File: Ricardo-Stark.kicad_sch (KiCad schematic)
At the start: 54 parts, among them J1 RBUS, U1 ESP32-S3, Y1 R940000171

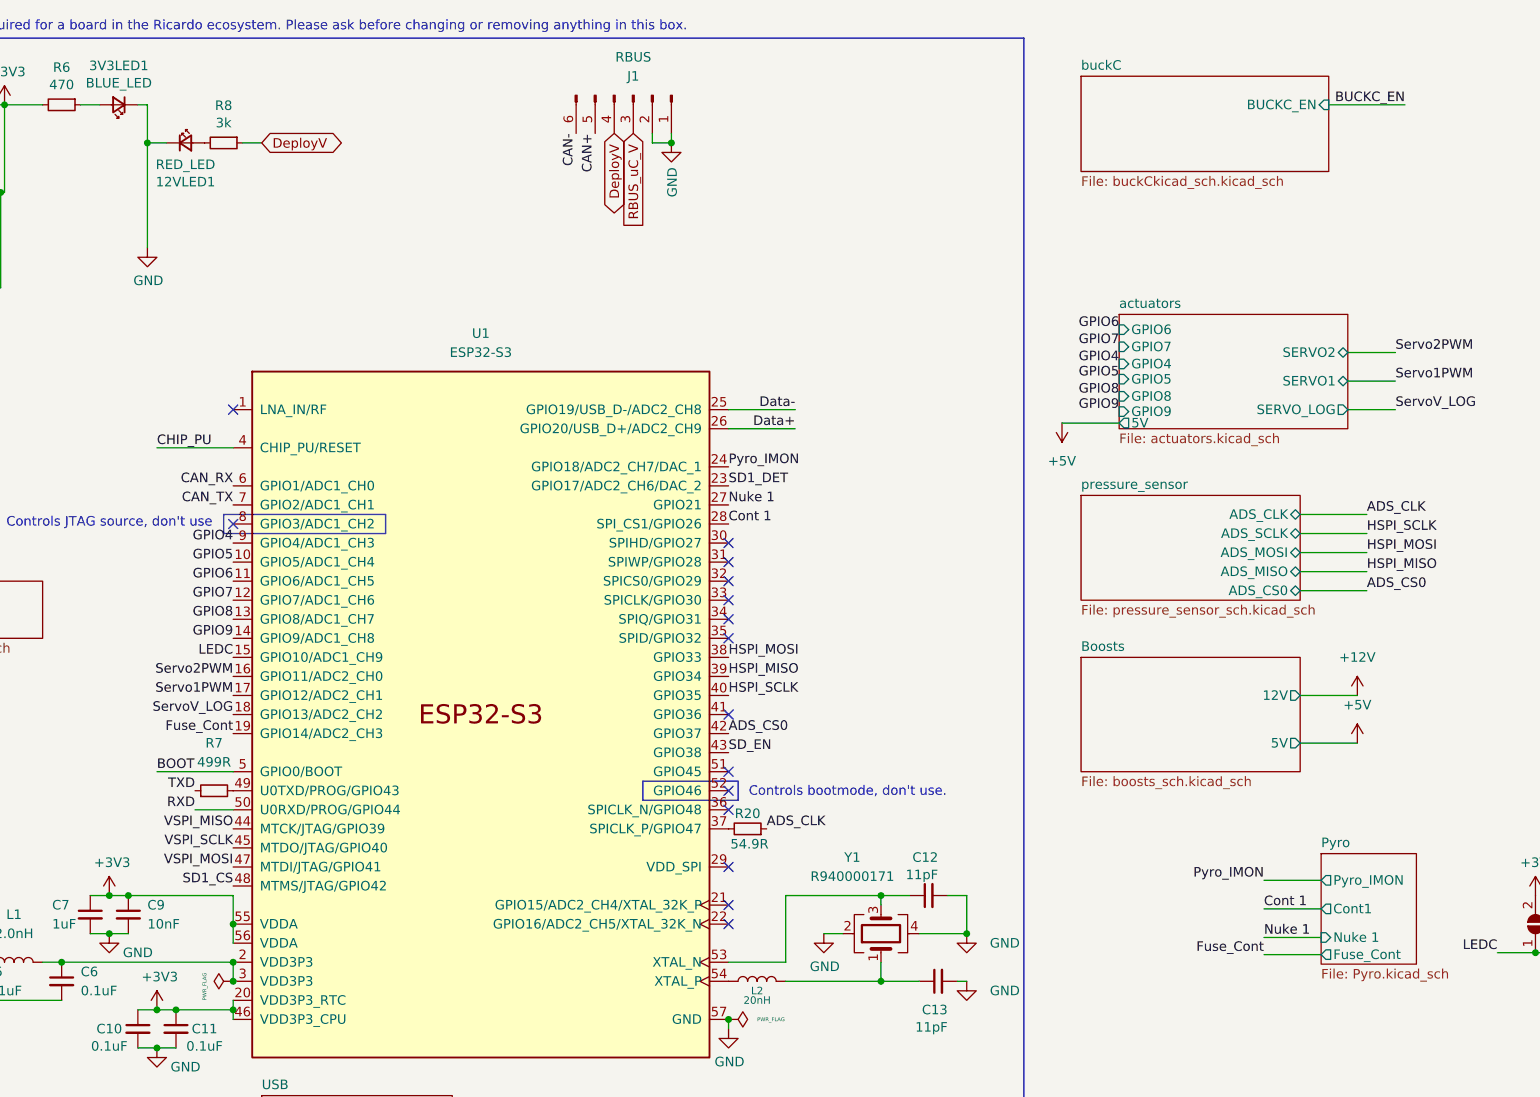
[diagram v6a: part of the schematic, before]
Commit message: reshuffled layout
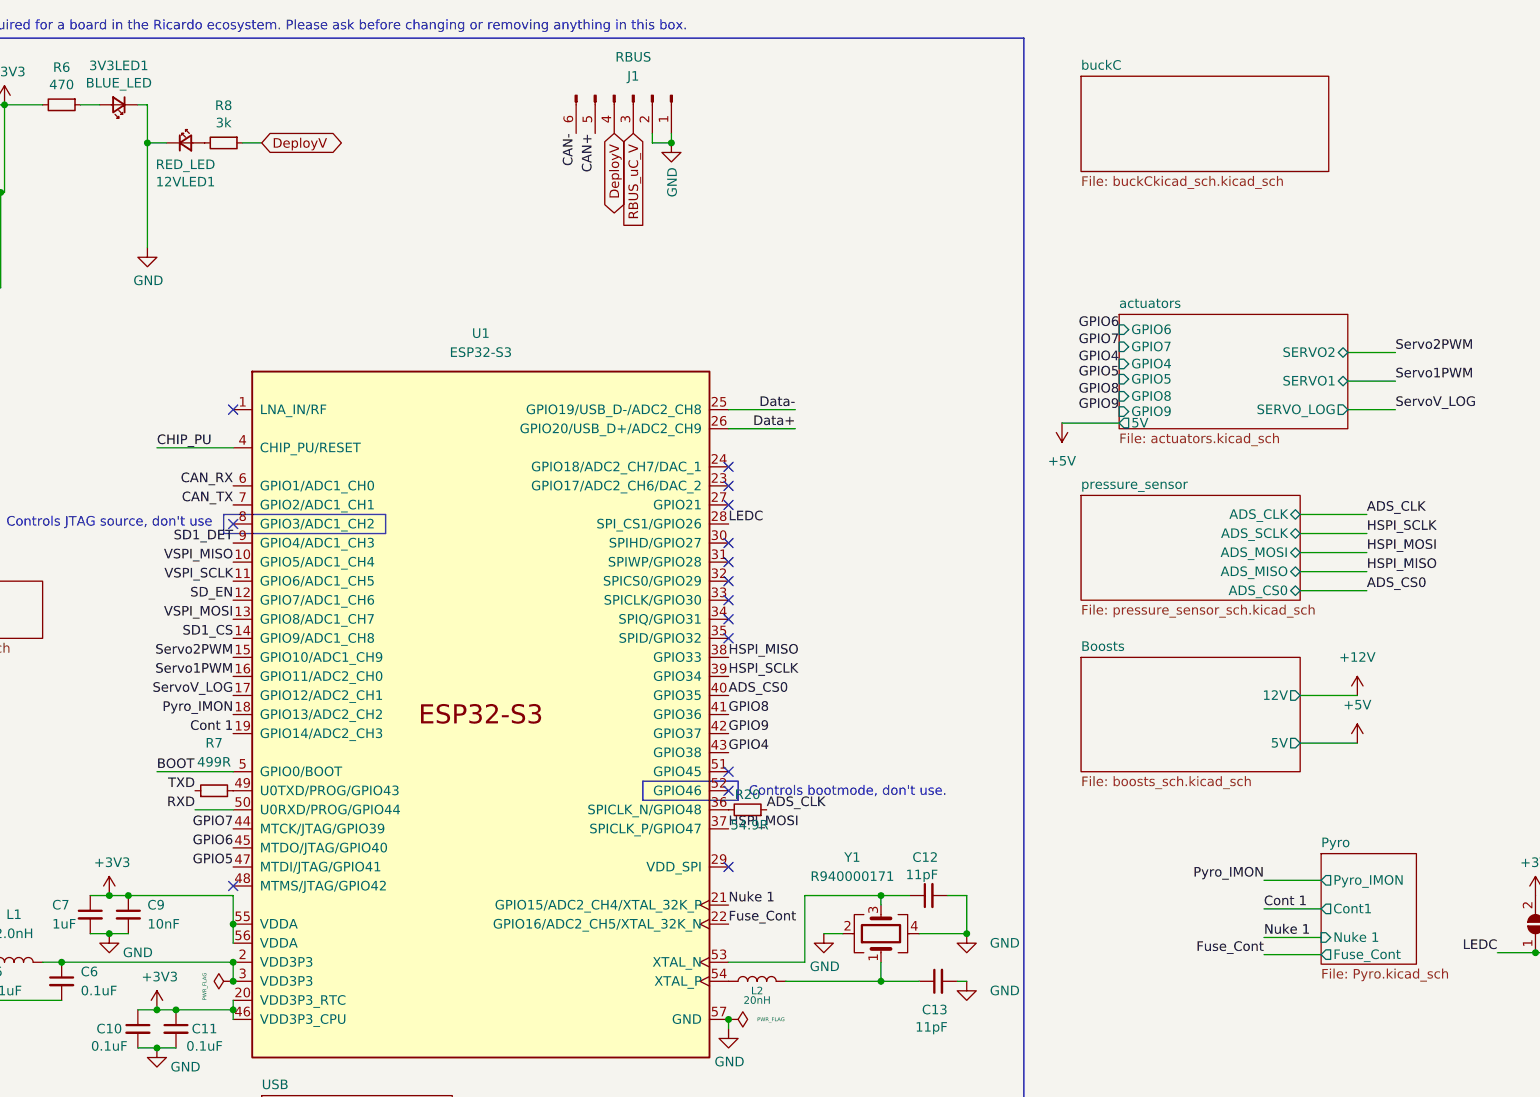
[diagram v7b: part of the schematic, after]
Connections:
- net ADS_CS0: now also U1.40 (GPIO35); no longer U1.42 (GPIO37)
- net Cont 1: now also U1.19 (GPIO14/ADC2_CH3); no longer U1.28 (SPI_CS1/GPIO26)
- net Fuse_Cont: now also U1.22 (GPIO16/ADC2_CH5/XTAL_32K_N); no longer U1.19 (GPIO14/ADC2_CH3)
- net GPIO4: now also U1.43 (GPIO38); no longer U1.9 (GPIO4/ADC1_CH3)
- net GPIO5: now also U1.47 (MTDI/JTAG/GPIO41); no longer U1.10 (GPIO5/ADC1_CH4)
- net GPIO6: now also U1.45 (MTDO/JTAG/GPIO40); no longer U1.11 (GPIO6/ADC1_CH5)
- net GPIO7: now also U1.44 (MTCK/JTAG/GPIO39); no longer U1.12 (GPIO7/ADC1_CH6)
- net GPIO8: now also U1.41 (GPIO36); no longer U1.13 (GPIO8/ADC1_CH7)
- net GPIO9: now also U1.42 (GPIO37); no longer U1.14 (GPIO9/ADC1_CH8)
- net HSPI_MISO: now also U1.38 (GPIO33); no longer U1.39 (GPIO34)
- net HSPI_MOSI: now also U1.37 (SPICLK_P/GPIO47); no longer U1.38 (GPIO33)
- net HSPI_SCLK: now also U1.39 (GPIO34); no longer U1.40 (GPIO35)
- net LEDC: now also U1.28 (SPI_CS1/GPIO26); no longer U1.15 (GPIO10/ADC1_CH9)
- net Nuke 1: now also U1.21 (GPIO15/ADC2_CH4/XTAL_32K_P); no longer U1.27 (GPIO21)
- net Pyro_IMON: now also U1.18 (GPIO13/ADC2_CH2); no longer U1.24 (GPIO18/ADC2_CH7/DAC_1)
- net SD1_CS: now also U1.14 (GPIO9/ADC1_CH8); no longer U1.48 (MTMS/JTAG/GPIO42)
- net SD1_DET: now also U1.9 (GPIO4/ADC1_CH3); no longer U1.23 (GPIO17/ADC2_CH6/DAC_2)
- net SD_EN: now also U1.12 (GPIO7/ADC1_CH6); no longer U1.43 (GPIO38)
- net Servo1PWM: now also U1.16 (GPIO11/ADC2_CH0); no longer U1.17 (GPIO12/ADC2_CH1)
- net Servo2PWM: now also U1.15 (GPIO10/ADC1_CH9); no longer U1.16 (GPIO11/ADC2_CH0)
- net ServoV_LOG: now also U1.17 (GPIO12/ADC2_CH1); no longer U1.18 (GPIO13/ADC2_CH2)
- net VSPI_MISO: now also U1.10 (GPIO5/ADC1_CH4); no longer U1.44 (MTCK/JTAG/GPIO39)
- net VSPI_MOSI: now also U1.13 (GPIO8/ADC1_CH7); no longer U1.47 (MTDI/JTAG/GPIO41)
- net VSPI_SCLK: now also U1.11 (GPIO6/ADC1_CH5); no longer U1.45 (MTDO/JTAG/GPIO40)
- net at R20.2: now also U1.36 (SPICLK_N/GPIO48); no longer U1.37 (SPICLK_P/GPIO47)
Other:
- sheet buckC ports: added none; removed BUCKC_EN
- moved on the sheet: R20
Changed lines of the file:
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@@
 	)
 	(no_connect
+		(at 135.89 69.85)
+	)
+	(no_connect
 		(at 135.89 82.55)
 	)
 	(no_connect
-		(at 135.89 130.81)
+		(at 135.89 72.39)
 	)
 	(no_connect
@@
 	)
 	(no_connect
-		(at 135.89 128.27)
-	)
-	(no_connect
 		(at 135.89 90.17)
 	)
@@
 	)
 	(no_connect
+		(at 135.89 74.93)
+	)
+	(no_connect
 		(at 135.89 87.63)
 	)
@@
 	)
 	(no_connect
-		(at 135.89 115.57)
-	)
-	(no_connect
 		(at 135.89 123.19)
 	)
@@
 	)
 	(no_connect
-		(at 135.89 102.87)
+		(at 69.85 125.73)
 	)
 	(wire
@@
 	(wire
 		(pts
-			(xy 143.51 135.89) (xy 143.51 127)
+			(xy 146.05 135.89) (xy 146.05 127)
 		)
 		(stroke
@@
 	(wire
 		(pts
-			(xy 215.9 21.59) (xy 226.06 21.59)
-		)
-		(stroke
-			(width 0)
-			(type default)
-		)
-	)
-	(wire
-		(pts
 			(xy 107.95 187.96) (xy 115.57 187.96)
 		)
@@
 	(wire
 		(pts
-			(xy 135.89 135.89) (xy 143.51 135.89)
+			(xy 135.89 135.89) (xy 146.05 135.89)
 		)
 		(stroke
@@
 	(wire
 		(pts
-			(xy 143.51 127) (xy 156.21 127)
+			(xy 146.05 127) (xy 156.21 127)
 		)
 		(stroke
@@
 	)
 	(label "SD1_DET"
-		(at 135.89 72.39 0)
-		(fields_autoplaced yes)
-		(effects
-			(font
-				(size 1.27 1.27)
-			)
-			(justify left bottom)
-		)
-	)
-	(label "BUCKC_EN"
-		(at 226.06 21.59 180)
+		(at 69.85 80.01 180)
 		(fields_autoplaced yes)
 		(effects
@@
 	)
 	(label "SD_EN"
-		(at 135.89 107.95 0)
+		(at 69.85 87.63 180)
 		(fields_autoplaced yes)
 		(effects
@@
 				(size 1.27 1.27)
 			)
-			(justify left bottom)
+			(justify right bottom)
 		)
 	)
@@
 	)
 	(label "Servo2PWM"
-		(at 69.85 97.79 180)
+		(at 69.85 95.25 180)
 		(fields_autoplaced yes)
 		(effects
@@
 	)
 	(label "Pyro_IMON"
-		(at 135.89 69.85 0)
+		(at 69.85 102.87 180)
 		(fields_autoplaced yes)
 		(effects
@@
 				(size 1.27 1.27)
 			)
-			(justify left bottom)
+			(justify right bottom)
 		)
 	)
@@
 	)
 	(label "Servo1PWM"
-		(at 69.85 100.33 180)
+		(at 69.85 97.79 180)
 		(fields_autoplaced yes)
 		(effects
@@
 	)
 	(label "GPIO7"
-		(at 69.85 87.63 180)
+		(at 69.85 118.11 180)
 		(fields_autoplaced yes)
 		(effects
@@
 	)
 	(label "VSPI_SCLK"
-		(at 69.85 120.65 180)
+		(at 69.85 85.09 180)
 		(fields_autoplaced yes)
 		(effects
@@
 	)
 	(label "SD1_CS"
-		(at 69.85 125.73 180)
+		(at 69.85 92.71 180)
 		(fields_autoplaced yes)
 		(effects
@@
 	)
 	(label "GPIO9"
-		(at 69.85 92.71 180)
+		(at 135.89 105.41 0)
 		(fields_autoplaced yes)
 		(effects
@@
 				(size 1.27 1.27)
 			)
-			(justify right bottom)
+			(justify left bottom)
 		)
 	)
 	(label "HSPI_SCLK"
-		(at 135.89 100.33 0)
+		(at 135.89 97.79 0)
 		(fields_autoplaced yes)
 		(effects
@@
 	)
 	(label "Fuse_Cont"
-		(at 69.85 105.41 180)
+		(at 135.89 130.81 0)
 		(fields_autoplaced yes)
 		(effects
@@
 				(size 1.27 1.27)
 			)
-			(justify right bottom)
+			(justify left bottom)
 		)
 	)
 	(label "VSPI_MISO"
-		(at 69.85 118.11 180)
+		(at 69.85 82.55 180)
 		(fields_autoplaced yes)
 		(effects
@@
 	)
 	(label "ADS_CLK"
-		(at 140.97 118.11 0)
+		(at 140.97 115.57 0)
 		(fields_autoplaced yes)
 		(effects
@@
 	)
 	(label "LEDC"
-		(at 69.85 95.25 180)
+		(at 135.89 77.47 0)
 		(fields_autoplaced yes)
 		(effects
@@
 				(size 1.27 1.27)
 			)
-			(justify right bottom)
+			(justify left bottom)
 		)
 	)
@@
 	)
 	(label "GPIO8"
-		(at 69.85 90.17 180)
+		(at 135.89 102.87 0)
 		(fields_autoplaced yes)
 		(effects
@@
 				(size 1.27 1.27)
 			)
-			(justify right bottom)
+			(justify left bottom)
 		)
 	)
@@
 	)
 	(label "Cont 1"
-		(at 135.89 77.47 0)
+		(at 69.85 105.41 180)
 		(fields_autoplaced yes)
 		(effects
@@
 				(size 1.27 1.27)
 			)
-			(justify left bottom)
+			(justify right bottom)
 		)
 	)
@@
 	)
 	(label "ServoV_LOG"
-		(at 69.85 102.87 180)
+		(at 69.85 100.33 180)
 		(fields_autoplaced yes)
 		(effects
@@
 	)
 	(label "GPIO5"
-		(at 69.85 82.55 180)
+		(at 69.85 123.19 180)
 		(fields_autoplaced yes)
 		(effects
@@
 	)
 	(label "GPIO6"
-		(at 69.85 85.09 180)
+		(at 69.85 120.65 180)
 		(fields_autoplaced yes)
 		(effects
@@
 	)
 	(label "ADS_CS0"
-		(at 135.89 105.41 0)
+		(at 135.89 100.33 0)
 		(fields_autoplaced yes)
 		(effects
@@
 	)
 	(label "Nuke 1"
-		(at 135.89 74.93 0)
+		(at 135.89 128.27 0)
 		(fields_autoplaced yes)
 		(effects
@@
 	)
 	(label "VSPI_MOSI"
-		(at 69.85 123.19 180)
+		(at 69.85 90.17 180)
 		(fields_autoplaced yes)
 		(effects
@@
 	)
 	(label "GPIO4"
-		(at 69.85 80.01 180)
+		(at 135.89 107.95 0)
 		(fields_autoplaced yes)
 		(effects
@@
 				(size 1.27 1.27)
 			)
-			(justify right bottom)
+			(justify left bottom)
 		)
 	)
@@
 	)
 	(label "HSPI_MISO"
-		(at 135.89 97.79 0)
+		(at 135.89 95.25 0)
 		(fields_autoplaced yes)
 		(effects
@@
 	)
 	(label "HSPI_MOSI"
-		(at 135.89 95.25 0)
+		(at 135.89 118.11 0)
 		(fields_autoplaced yes)
 		(effects
@@
 	(symbol
 		(lib_id "Device:R_Small")
-		(at 138.43 118.11 270)
+		(at 138.43 115.57 270)
 		(mirror x)
 		(unit 1)
@@
 		(dnp no)
 		(property "Reference" "R20"
-			(at 138.43 116.078 90)
+			(at 138.43 113.538 90)
 			(effects
 				(font
@@
 		)
 		(property "Value" "54.9R"
-			(at 138.684 120.142 90)
+			(at 138.684 117.602 90)
 			(effects
 				(font
@@
 		)
 		(property "Footprint" "Resistor_SMD:R_0402_1005Metric"
-			(at 138.43 118.11 0)
+			(at 138.43 115.57 0)
 			(effects
 				(font
@@
 		)
 		(property "Datasheet" "~"
-			(at 138.43 118.11 0)
+			(at 138.43 115.57 0)
 			(effects
 				(font
@@
 		)
 		(property "Description" ""
-			(at 138.43 118.11 0)
+			(at 138.43 115.57 0)
 			(effects
 				(font
@@
 			)
 		)
-		(pin "BUCKC_EN" input
-			(at 215.9 21.59 0)
-			(effects
-				(font
-					(size 1.27 1.27)
-				)
-				(justify right)
-			)
-		)

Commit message: more changes
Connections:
- net SD_EN: now also U1.10 (GPIO5/ADC1_CH4); no longer U1.12 (GPIO7/ADC1_CH6)
- net VSPI_MISO: now also U1.11 (GPIO6/ADC1_CH5); no longer U1.10 (GPIO5/ADC1_CH4)
- net VSPI_SCLK: now also U1.12 (GPIO7/ADC1_CH6); no longer U1.11 (GPIO6/ADC1_CH5)
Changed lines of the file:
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@@
 	)
 	(label "SD_EN"
-		(at 69.85 87.63 180)
+		(at 69.85 82.55 180)
 		(fields_autoplaced yes)
 		(effects
@@
 	)
 	(label "VSPI_SCLK"
-		(at 69.85 85.09 180)
+		(at 69.85 87.63 180)
 		(fields_autoplaced yes)
 		(effects
@@
 	)
 	(label "VSPI_MISO"
-		(at 69.85 82.55 180)
-		(fields_autoplaced yes)
-		(effects
+		(at 69.85 85.09 180)
+		(fields_autoplaced yes)
+		(effects
